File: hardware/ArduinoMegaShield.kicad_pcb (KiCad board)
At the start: 2 copper layers, 48 parts, among them P1 CONN_01X02, P10 CONN_01X02, P11 CONN_01X02, P12 CONN_01X02, P13 CONN_01X02, P14 CONN_01X02, P15 CONN_01X02, P16 CONN_01X02, P17 CONN_01X02, P18 CONN_01X02, P19 CONN_01X02, P2 CONN_01X02, P20 CONN_01X02, P21 CONN_01X02, P22 CONN_01X02, P3 CONN_01X02, P4 CONN_01X02, P5 CONN_01X02, P6 CONN_01X02, P7 CONN_01X02, P8 CONN_01X02, P9 CONN_01X02, U1 A4988, U2 A4988, U3 A4988

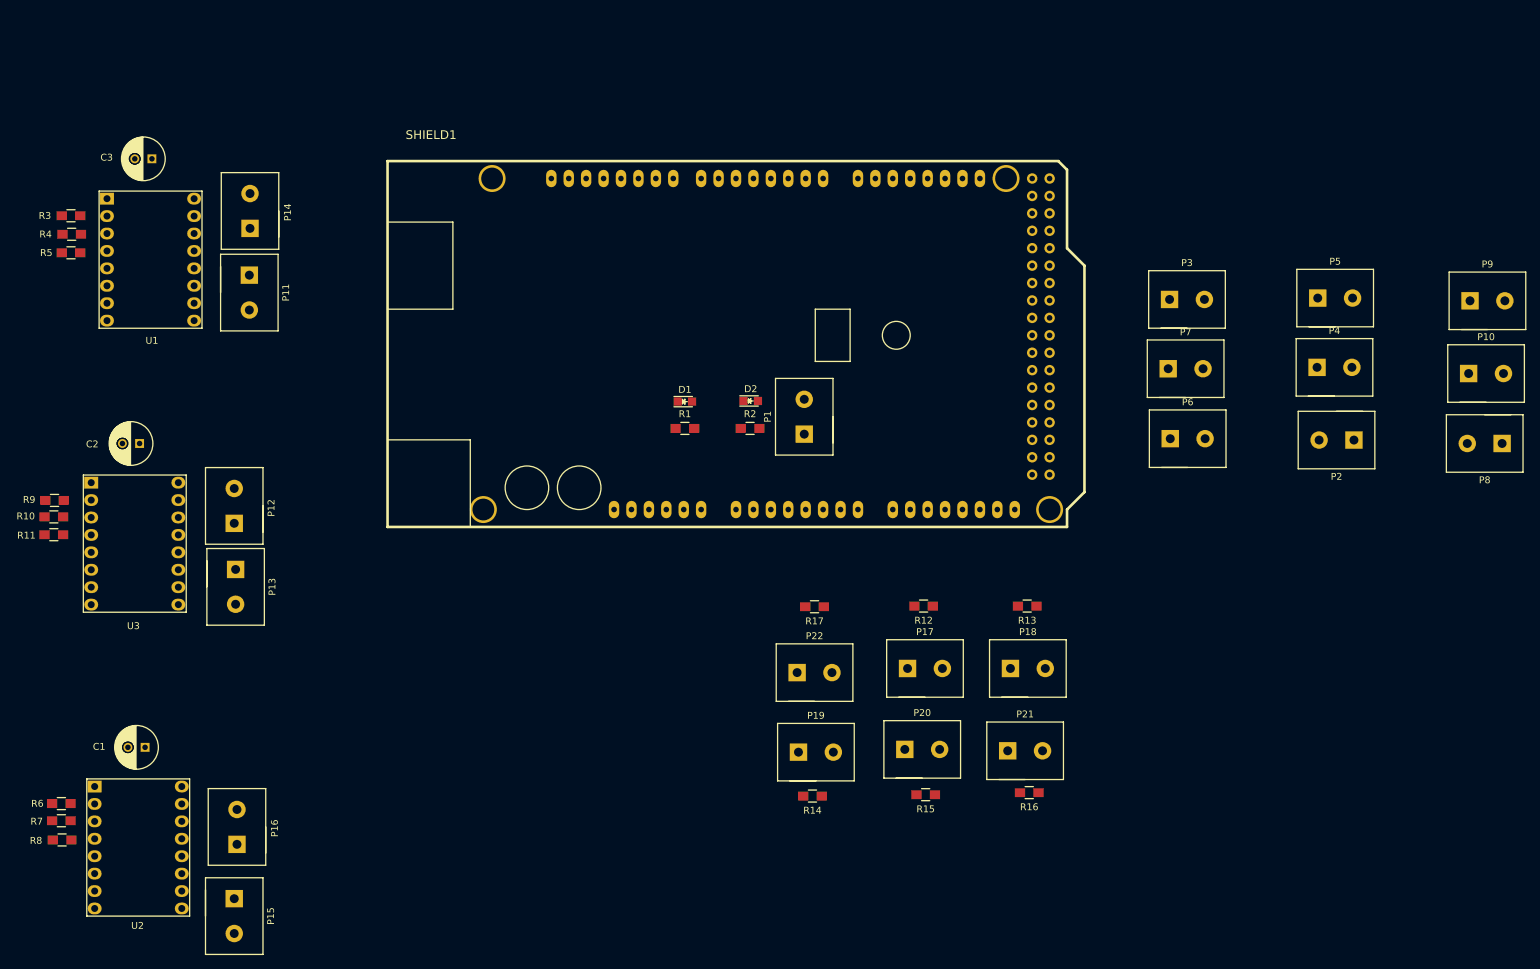
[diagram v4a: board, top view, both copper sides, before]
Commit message: moved connectors to separate sheet and started board layout
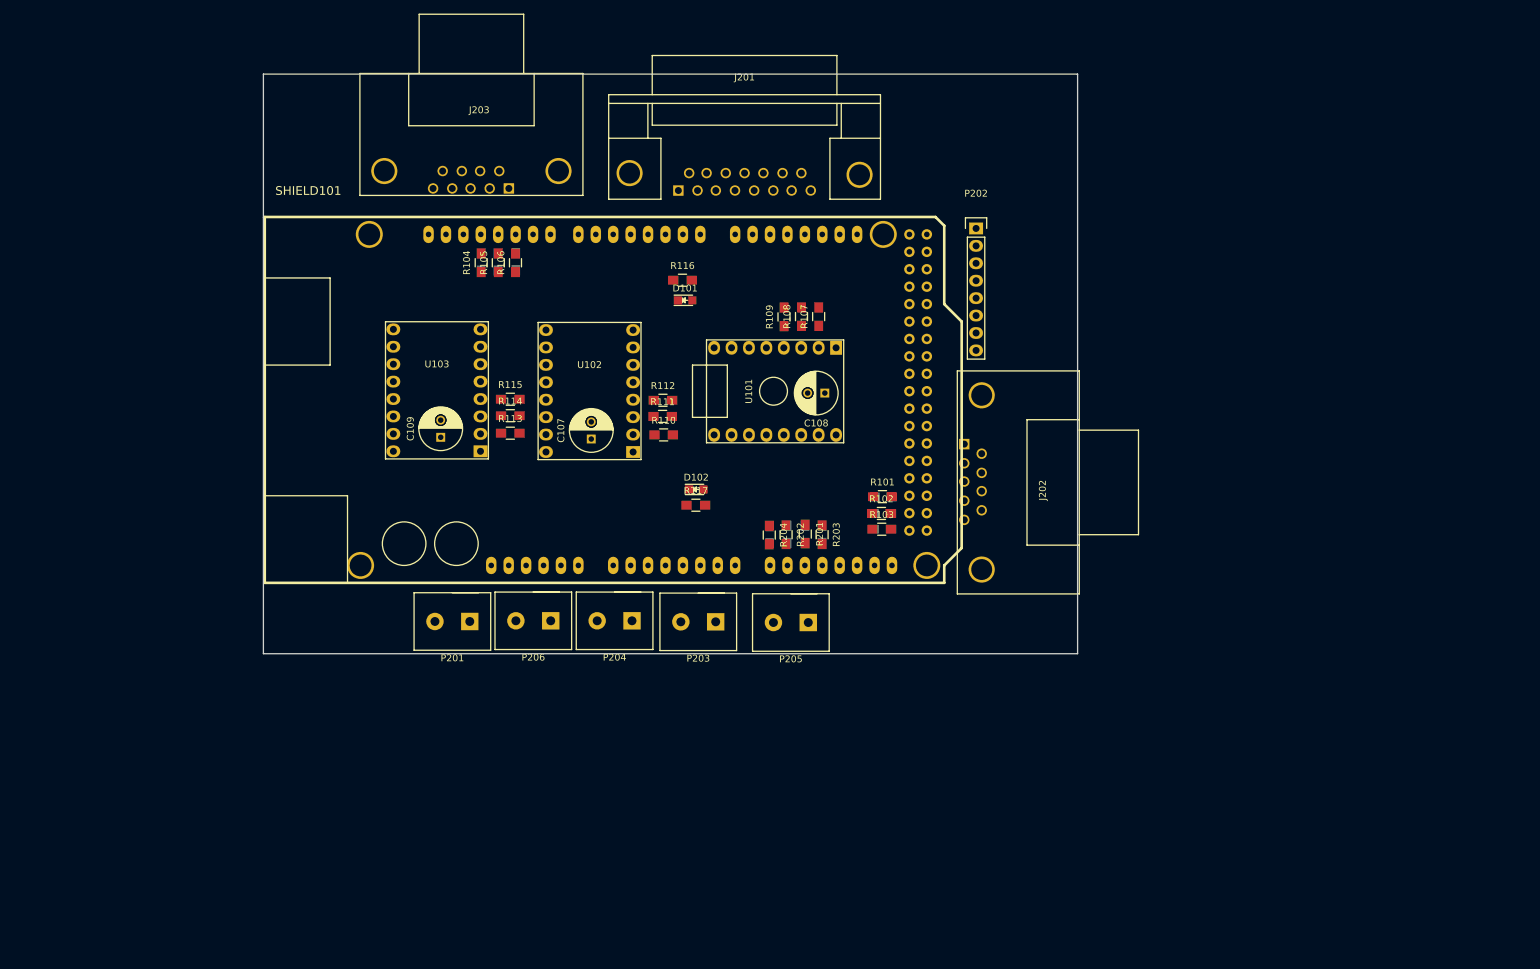
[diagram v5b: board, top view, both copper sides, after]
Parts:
- removed C1, C2, C3: 100u, Capacitors_THT:C_Radial_D6.3_L11.2_P2.5
- removed D1: G LED, LEDs:LED_0805
- removed D2: R LED, LEDs:LED_0805
- removed P1, P10, P11, P12, P13, P14, P15, P16, P17, P18, P19, P2, P20, P21, P22, P3, P4, P5, P6, P7, P8, P9: CONN_01X02, 6axis:Terminal_Block_200_mil
- removed R1: 560R, Resistors_SMD:R_0805_HandSoldering
- removed R10, R11, R12, R13, R14, R15, R16, R17, R3, R4, R5, R6, R7, R8, R9: NOPOP, Resistors_SMD:R_0805_HandSoldering
- removed R2: 2K, Resistors_SMD:R_0805_HandSoldering
- removed SHIELD1: ARDUINO_MEGA_SHIELD, arduino-shields:ARDUINO_MEGA_SHIELD
- removed U1, U2, U3: A4988, 6axis:A4988
- added C101: 0.1u, Capacitors_SMD:C_0805_HandSoldering, B.Cu at (164.1, 121.4)
- added C102: 0.1u, Capacitors_SMD:C_0805_HandSoldering, B.Cu at (164.0, 123.8)
- added C103: 0.1u, Capacitors_SMD:C_0805_HandSoldering, B.Cu at (164.0, 126.1)
- added C104: 0.1u, Capacitors_SMD:C_0805_HandSoldering, B.Cu at (105.5, 87.2)
- added C105: 0.1u, Capacitors_SMD:C_0805_HandSoldering, B.Cu at (108.0, 87.2)
- added C106: 0.1u, Capacitors_SMD:C_0805_HandSoldering, B.Cu at (110.5, 87.1)
- added C107: 100u, Capacitors_THT:C_Radial_D6.3_L11.2_P2.5, F.Cu at (121.5, 113.0)
- added C108: 100u, Capacitors_THT:C_Radial_D6.3_L11.2_P2.5, F.Cu at (155.6, 106.2)
- added C109: 100u, Capacitors_THT:C_Radial_D6.3_L11.2_P2.5, F.Cu at (99.6, 112.7)
- added C201: 0.1u, Capacitors_SMD:C_0805_HandSoldering, B.Cu at (152.7, 126.8)
- added C202: 0.1u, Capacitors_SMD:C_0805_HandSoldering, B.Cu at (150.1, 126.8)
- added C203: 0.1u, Capacitors_SMD:C_0805_HandSoldering, B.Cu at (155.2, 126.8)
- added C204: 0.1u, Capacitors_SMD:C_0805_HandSoldering, B.Cu at (147.6, 126.9)
- added D101: G LED, LEDs:LED_0805, F.Cu at (135.2, 92.7)
- added D102: R LED, LEDs:LED_0805, F.Cu at (136.8, 120.3)
- added J201: DB15, Connectors:DB15FC, F.Cu at (143.9, 75.5)
- added J202: DB9, Connectors:DB9FC, F.Cu at (177.2, 119.2)
- added J203: DB9, Connectors:DB9MC, F.Cu at (104.0, 75.2)
- added P201: CONN_01X02, 6axis:Terminal_Block_200_mil, F.Cu at (101.3, 139.6)
- added P202: CONN_01X08, Pin_Headers:Pin_Header_Straight_1x08, F.Cu at (177.7, 82.2)
- added P203: CONN_01X02, 6axis:Terminal_Block_200_mil, F.Cu at (137.2, 139.6)
- added P204: CONN_01X02, 6axis:Terminal_Block_200_mil, F.Cu at (125.0, 139.4)
- added P205: CONN_01X02, 6axis:Terminal_Block_200_mil, F.Cu at (150.7, 139.7)
- added P206: CONN_01X02, 6axis:Terminal_Block_200_mil, F.Cu at (113.1, 139.4)
- added R101: 4.7K, Resistors_SMD:R_0805_HandSoldering, F.Cu at (164.0, 121.3)
- added R102: 4.7K, Resistors_SMD:R_0805_HandSoldering, F.Cu at (163.8, 123.8)
- added R103: 4.7K, Resistors_SMD:R_0805_HandSoldering, F.Cu at (163.9, 126.1)
- added R104: 4.7K, Resistors_SMD:R_0805_HandSoldering, F.Cu at (105.5, 87.2)
- added R105: 4.7K, Resistors_SMD:R_0805_HandSoldering, F.Cu at (108.0, 87.2)
- added R106: 4.7K, Resistors_SMD:R_0805_HandSoldering, F.Cu at (110.5, 87.2)
- added R107: NOPOP, Resistors_SMD:R_0805_HandSoldering, F.Cu at (154.7, 95.1)
- added R108: NOPOP, Resistors_SMD:R_0805_HandSoldering, F.Cu at (152.2, 95.1)
- added R109: NOPOP, Resistors_SMD:R_0805_HandSoldering, F.Cu at (149.7, 95.2)
- added R110: NOPOP, Resistors_SMD:R_0805_HandSoldering, F.Cu at (132.1, 112.3)
- added R111: NOPOP, Resistors_SMD:R_0805_HandSoldering, F.Cu at (131.9, 109.7)
- added R112: NOPOP, Resistors_SMD:R_0805_HandSoldering, F.Cu at (132.0, 107.3)
- added R113: NOPOP, Resistors_SMD:R_0805_HandSoldering, F.Cu at (109.8, 112.1)
- added R114: NOPOP, Resistors_SMD:R_0805_HandSoldering, F.Cu at (109.8, 109.5)
- added R115: NOPOP, Resistors_SMD:R_0805_HandSoldering, F.Cu at (109.8, 107.2)
- added R116: 560R, Resistors_SMD:R_0805_HandSoldering, F.Cu at (134.8, 89.8)
- added R117: 2K, Resistors_SMD:R_0805_HandSoldering, F.Cu at (136.8, 122.6)
- added R201: 4.7K, Resistors_SMD:R_0805_HandSoldering, F.Cu at (152.8, 126.8)
- added R202: 4.7K, Resistors_SMD:R_0805_HandSoldering, F.Cu at (149.9, 126.9)
- added R203: 4.7K, Resistors_SMD:R_0805_HandSoldering, F.Cu at (155.2, 126.9)
- added R204: 4.7K, Resistors_SMD:R_0805_HandSoldering, F.Cu at (147.5, 127.0)
- added SHIELD101: ARDUINO_MEGA_SHIELD, arduino-shields:ARDUINO_MEGA_SHIELD, F.Cu at (74.0, 133.9)
- added U101: A4988, 6axis:A4988, F.Cu at (148.3, 106.0)
- added U102: A4988, 6axis:A4988, F.Cu at (121.3, 106.0)
- added U103: A4988, 6axis:A4988, F.Cu at (99.0, 105.8)
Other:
- board outline added: 118.7 x 84.5 mm

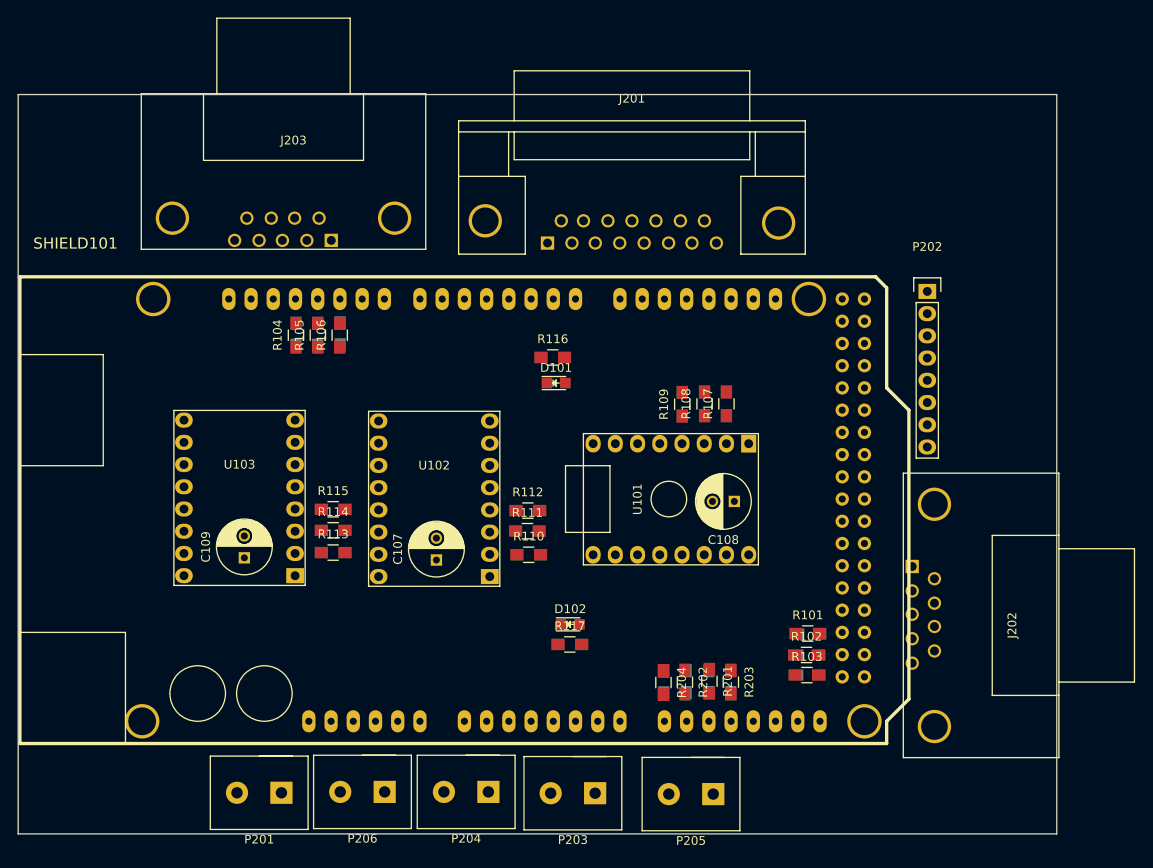
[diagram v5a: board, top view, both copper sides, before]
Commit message: changed connector footprints and added rotory dip switch footprint
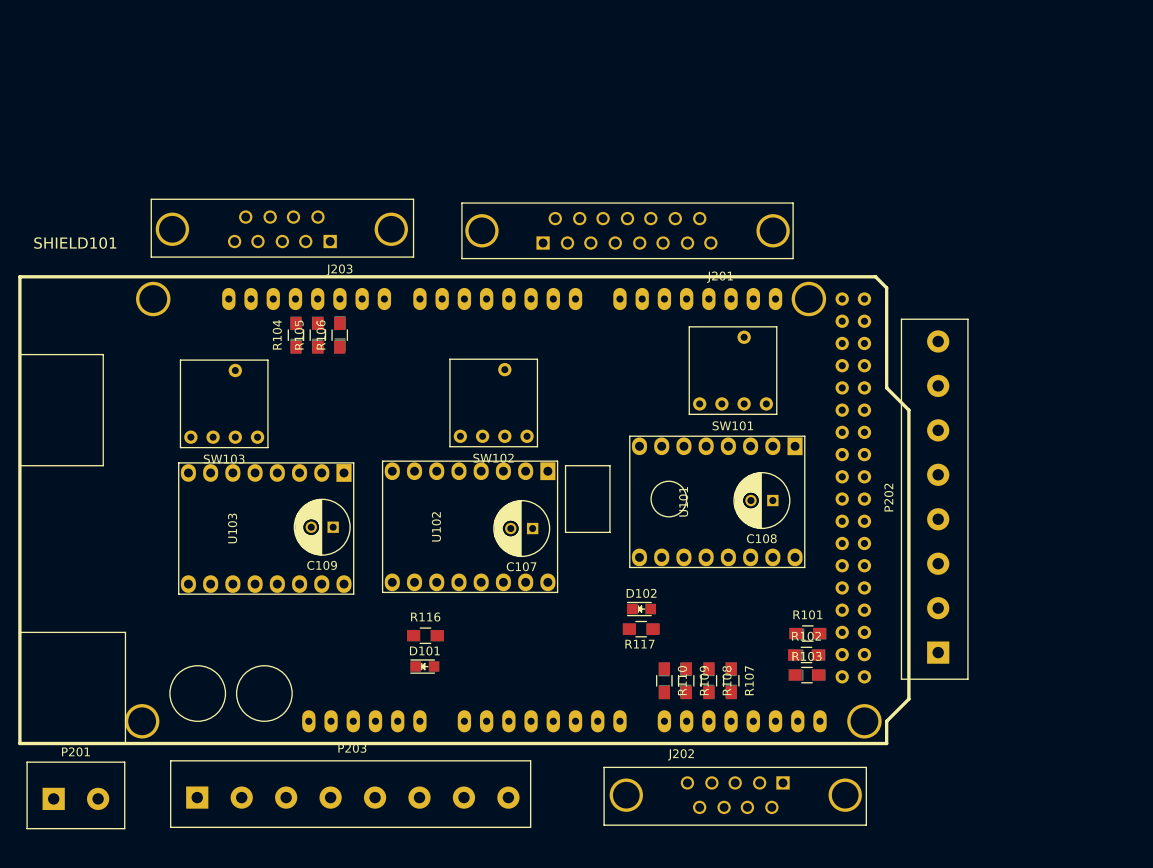
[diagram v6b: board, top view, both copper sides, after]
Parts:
- removed C201, C202, C203, C204: 0.1u, Capacitors_SMD:C_0805_HandSoldering
- removed P204, P205, P206: CONN_01X02, 6axis:Terminal_Block_200_mil
- removed R111, R112, R113, R114, R115: NOPOP, Resistors_SMD:R_0805_HandSoldering
- removed R201, R202, R203, R204: 4.7K, Resistors_SMD:R_0805_HandSoldering
- added C110: 0.1u, Capacitors_SMD:C_0805_HandSoldering, B.Cu at (155.2, 126.7)
- added C111: 0.1u, Capacitors_SMD:C_0805_HandSoldering, B.Cu at (152.7, 126.7)
- added C112: 0.1u, Capacitors_SMD:C_0805_HandSoldering, B.Cu at (150.1, 126.7)
- added C113: 0.1u, Capacitors_SMD:C_0805_HandSoldering, B.Cu at (147.6, 126.8)
- added SW101: SW_Coded, 6axis:S-1010A, F.Cu at (155.4, 91.3)
- added SW102: SW_Coded, 6axis:S-1010A, F.Cu at (128.1, 95.0)
- added SW103: SW_Coded, 6axis:S-1010A, F.Cu at (97.3, 95.1)
- J201: footprint Connectors:DB15FC -> Connectors:DB15FD
- J202: footprint Connectors:DB9FC -> Connectors:DB9FD
- J203: footprint Connectors:DB9MC -> Connectors:DB9MD
- P202: footprint Pin_Headers:Pin_Header_Straight_1x08 -> 6axis:Terminal_Block_200_mil_8pos
- P203: value CONN_01X02 -> CONN_01X08; footprint 6axis:Terminal_Block_200_mil -> 6axis:Terminal_Block_200_mil_8pos
- R107, R108, R109, R110: value NOPOP -> 4.7K
- moved D101 35.7 mm to (120.2, 125.1)
- moved R116 35.0 mm to (120.3, 121.6)
- moved R107 31.7 mm to (155.2, 126.8), turned to 270 degrees
- moved R108 31.7 mm to (152.7, 126.8), turned to 270 degrees
- moved R109 31.6 mm to (150.1, 126.8), turned to 270 degrees
- moved J202 29.9 mm to (155.7, 139.9), turned to 0 degrees
- moved P203 25.2 mm to (112.0, 140.1), turned to 0 degrees
- moved P202 23.5 mm to (178.9, 105.8), turned to 90 degrees
- moved R110 21.2 mm to (147.6, 126.8), turned to 270 degrees
- moved P201 21.0 mm to (80.3, 140.2), turned to 0 degrees
- moved C107 11.6 mm to (132.6, 109.3), turned to 180 degrees
- moved C109 10.7 mm to (109.8, 109.2), turned to 180 degrees
- moved D102 8.34 mm to (145.0, 118.5)
- moved R117 8.34 mm to (144.9, 120.8)
- moved U101 5.31 mm to (153.7, 106.3)
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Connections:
- C104 pad 1: /Z_LIMIT -> GND
- C104 pad 2: GND -> /X_LIMIT
- C105 pad 1: /Y_LIMIT -> GND
- C105 pad 2: GND -> /Z_LIMIT
- C106 pad 1: /X_LIMIT -> GND
- C106 pad 2: GND -> /Y_LIMIT
- R104 pad 2: /Z_LIMIT -> /X_LIMIT
- R106 pad 2: /X_LIMIT -> /Z_LIMIT
- R107 pad 1: Net-(R107-Pad1) -> +5V
- R107 pad 2: +5V -> /SAFETY_DOOR
- R108 pad 1: Net-(R108-Pad1) -> +5V
- R108 pad 2: +5V -> /CYCLE_START
- R109 pad 1: Net-(R109-Pad1) -> +5V
- R109 pad 2: +5V -> /FEED_HOLD
- R110 pad 1: Net-(R110-Pad1) -> +5V
- R110 pad 2: +5V -> /RESET
- U101 pad 2: Net-(R107-Pad1) -> Net-(SW101-Pad2)
- U101 pad 3: Net-(R108-Pad1) -> Net-(SW101-Pad3)
- U101 pad 4: Net-(R109-Pad1) -> Net-(SW101-Pad4)
- U102 pad 2: Net-(R110-Pad1) -> Net-(SW102-Pad2)
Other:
- board outline removed
